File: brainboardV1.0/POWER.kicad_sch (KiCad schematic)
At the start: 16 parts, among them J21 Conn_01x01, J22 Conn_01x01, J23 Conn_01x01, U21 LD1117S18TR_SOT223

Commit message: finalized PCB, changed file names
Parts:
- removed J21, J23: Conn_01x01, Connector_PinSocket_2.54mm:PinSocket_1x01_P2.54mm_Vertical, symbol Connector_Generic:Conn_01x01
- added J24, J25: Conn_01x01, Connector_Wire:SolderWire-2sqmm_1x01_D2mm_OD3.9mm, symbol Connector_Generic:Conn_01x01
- added U22: my_buck_boost, Converter_DCDC:my_buck_boost, symbol two_motor_driver-rescue:my_buck_boost-Regulator_Switching
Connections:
- net +5V: now also U22.7 (Reg_out), U22.8 (Reg_out); no longer SW_SPDT21.1 (A)
- net GND: now also J24.1 (Pin_1), U22.1 (IN_-), U22.2 (IN_-), U22.5 (Reg_GND), U22.6 (Reg_GND)
- net VESC1_VCC renamed MESC1_VCC
- net VESC_+5V renamed Vcc
- net Vcc: now also J25.1 (Pin_1)
- new net: SW_SPDT21.1 (A), U22.3 (IN_+), U22.4 (IN_+)
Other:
- moved on the sheet: SW_SPDT21

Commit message: finalizing PCB
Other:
- moved on the sheet: J22
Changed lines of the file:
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@@
 	(global_label "+3.3V"
 		(shape input)
-		(at 130.81 93.98 180)
+		(at 154.94 106.68 180)
 		(effects
 			(font
@@
 		)
 		(property "Intersheetrefs" "${INTERSHEET_REFS}"
-			(at 130.81 93.98 0)
+			(at 154.94 106.68 0)
 			(effects
 				(font
@@
 	(symbol
 		(lib_id "Connector_Generic:Conn_01x01")
-		(at 135.89 93.98 0)
+		(at 160.02 106.68 0)
 		(unit 1)
 		(exclude_from_sim no)
@@
 		(fields_autoplaced yes)
 		(property "Reference" "J22"
-			(at 138.43 93.9799 0)
+			(at 162.56 106.6799 0)
 			(effects
 				(font
@@
 		)
 		(property "Value" "Conn_01x01"
-			(at 138.43 95.2499 0)
+			(at 162.56 107.9499 0)
 			(effects
 				(font
@@
 		)
 		(property "Footprint" "Connector_PinSocket_2.54mm:PinSocket_1x01_P2.54mm_Vertical"
-			(at 135.89 93.98 0)
+			(at 160.02 106.68 0)
 			(effects
 				(font
@@
 		)
 		(property "Datasheet" "~"
-			(at 135.89 93.98 0)
+			(at 160.02 106.68 0)
 			(effects
 				(font
@@
 		)
 		(property "Description" "Generic connector, single row, 01x01, script generated (kicad-library-utils/schlib/autogen/connector/)"
-			(at 135.89 93.98 0)
-			(effects
-				(font
+			(at 160.02 106.68 0)
+			(effects
+				(font

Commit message: First board ordered from JLCPCB
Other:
- note added: "Voltage divider Not implemented"
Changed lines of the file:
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@@
+		)
+	)
+	(text "Voltage divider\nNot implemented"
+		(exclude_from_sim no)
+		(at 78.486 99.06 0)
+		(effects
+			(font
+				(size 1.27 1.27)
+			)
+			(justify left)
 		)
 	)

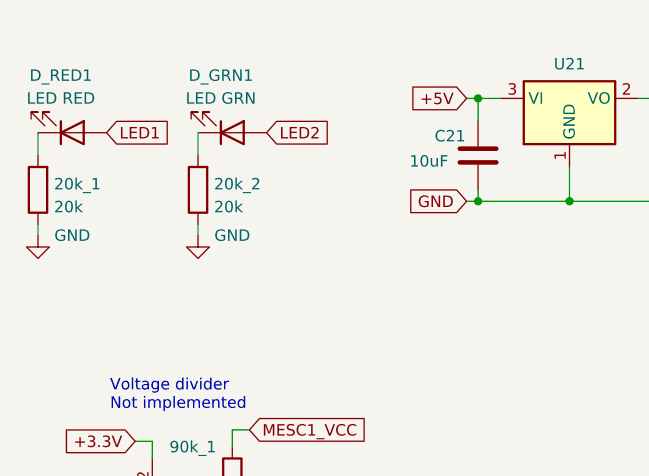
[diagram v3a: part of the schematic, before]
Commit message: update grn LED resistor
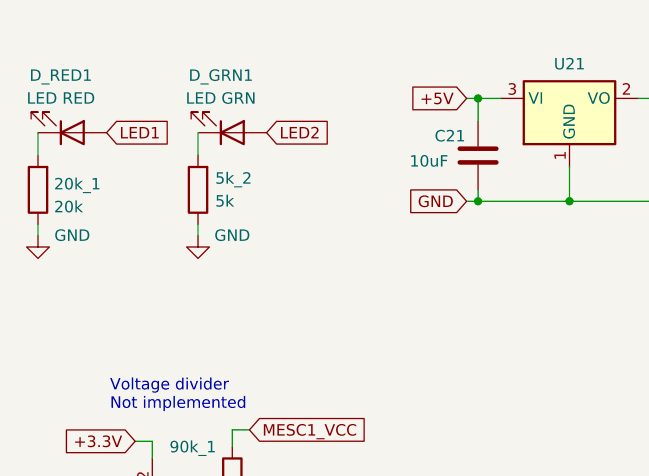
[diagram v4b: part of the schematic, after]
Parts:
- 5k_2: renamed from 20k_2; value 20k -> 5k
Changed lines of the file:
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@@
 		(dnp no)
 		(fields_autoplaced yes)
-		(property "Reference" "20k_2"
-			(at 90.043 75.565 0)
+		(property "Reference" "5k_2"
+			(at 90.17 74.9299 0)
 			(effects
 				(font
@@
 			)
 		)
-		(property "Value" "20k"
-			(at 90.043 78.105 0)
+		(property "Value" "5k"
+			(at 90.17 77.4699 0)
 			(effects
 				(font
@@
 			(project "MESC_brain_board"
 				(path "/8920b97c-b80b-47c5-aaa4-fe68c48cd11a/165c0a2c-8484-48b2-be46-c9f57520b95f"
-					(reference "20k_2")
+					(reference "5k_2")
 					(unit 1)
 				)
